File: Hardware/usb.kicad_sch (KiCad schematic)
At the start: 4 parts, among them J3 USB_C_Receptacle_USB2.0

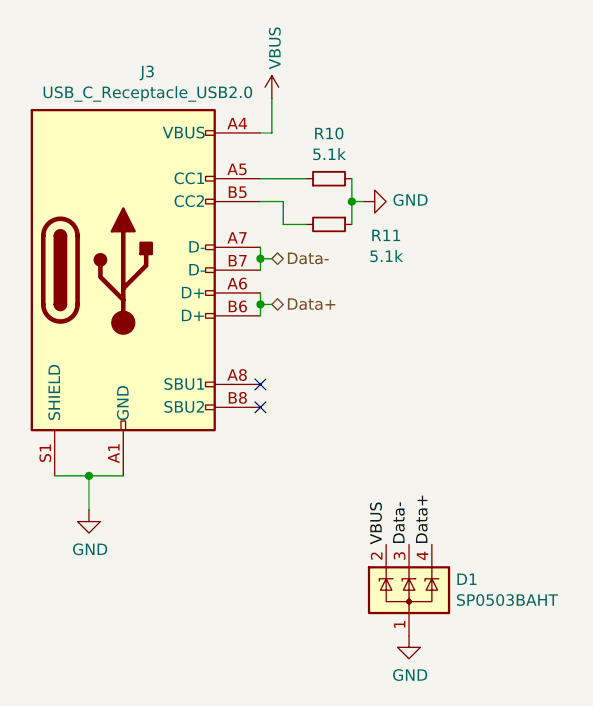
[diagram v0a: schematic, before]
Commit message: Initial changes : removed efuse in place of a current sensor and hardware fuse xt60
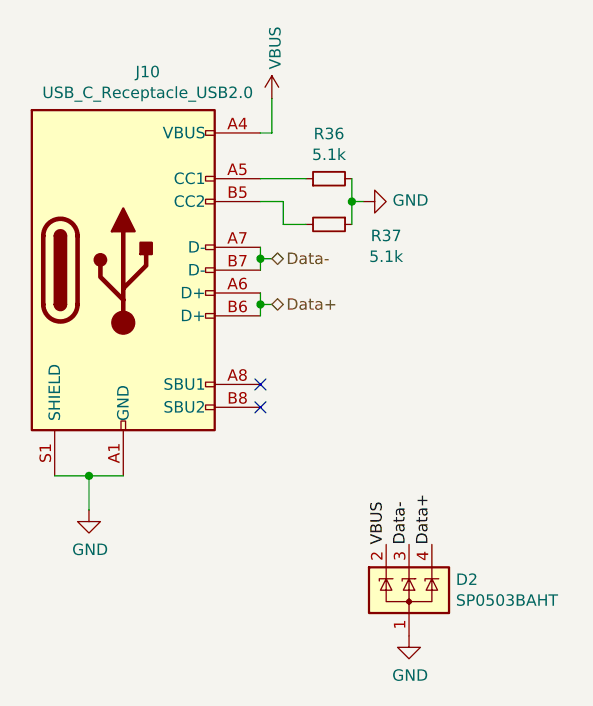
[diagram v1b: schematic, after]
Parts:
- renumbered D1 to D2, J3 to J10, R10 to R36, R11 to R37
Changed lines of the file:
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@@
 (kicad_sch
-	(version 20231120)
+	(version 20250114)
 	(generator "eeschema")
-	(generator_version "8.0")
+	(generator_version "9.0")
 	(paper "A4")
 	(junction
@@
 	(label "Data-"
 		(at 156.464 121.158 90)
-		(fields_autoplaced yes)
 		(effects
 			(font
@@
 	(label "Data+"
 		(at 159.004 121.158 90)
-		(fields_autoplaced yes)
 		(effects
 			(font
@@
 	(label "VBUS"
 		(at 153.924 121.158 90)
-		(fields_autoplaced yes)
 		(effects
 			(font
@@
 		(shape bidirectional)
 		(at 141.224 89.408 0)
-		(fields_autoplaced yes)
 		(effects
 			(font
@@
 		(shape bidirectional)
 		(at 141.224 94.488 0)
-		(fields_autoplaced yes)
 		(effects
 			(font
@@
 		(on_board yes)
 		(dnp no)
-		(property "Reference" "#PWR0129"
+		(property "Reference" "#PWR070"
 			(at 156.464 137.668 0)
 			(effects
@@
 			(project "PDU"
 				(path "/e63e39d7-6ac0-4ffd-8aa3-1841a4541b55/7369ceff-38ea-4740-9245-fda19d5ff608"
-					(reference "#PWR0129")
+					(reference "#PWR070")
 					(unit 1)
 				)
@@
 		(on_board yes)
 		(dnp no)
-		(property "Reference" "#PWR0134"
+		(property "Reference" "#PWR068"
 			(at 141.224 75.438 0)
 			(effects
@@
 			(project "PDU"
 				(path "/e63e39d7-6ac0-4ffd-8aa3-1841a4541b55/7369ceff-38ea-4740-9245-fda19d5ff608"
-					(reference "#PWR0134")
+					(reference "#PWR068")
 					(unit 1)
 				)
@@
 		(on_board yes)
 		(dnp no)
-		(property "Reference" "#PWR0131"
+		(property "Reference" "#PWR069"
 			(at 157.734 83.058 0)
 			(effects
@@
 			(project "PDU"
 				(path "/e63e39d7-6ac0-4ffd-8aa3-1841a4541b55/7369ceff-38ea-4740-9245-fda19d5ff608"
-					(reference "#PWR0131")
+					(reference "#PWR069")
 					(unit 1)
 				)
@@
 		(on_board yes)
 		(dnp no)
-		(property "Reference" "J3"
+		(property "Reference" "J10"
 			(at 127.4318 68.6562 0)
 			(effects
@@
 			(project "PDU"
 				(path "/e63e39d7-6ac0-4ffd-8aa3-1841a4541b55/7369ceff-38ea-4740-9245-fda19d5ff608"
-					(reference "J3")
+					(reference "J10")
 					(unit 1)
 				)
@@
 		(on_board yes)
 		(dnp no)
-		(property "Reference" "R10"
+		(property "Reference" "R36"
 			(at 147.574 75.5396 90)
 			(effects
@@
 			(project "PDU"
 				(path "/e63e39d7-6ac0-4ffd-8aa3-1841a4541b55/7369ceff-38ea-4740-9245-fda19d5ff608"
-					(reference "R10")
+					(reference "R36")
 					(unit 1)
 				)
@@
 		(on_board yes)
 		(dnp no)
-		(property "Reference" "#PWR0126"
+		(property "Reference" "#PWR067"
 			(at 120.904 123.698 0)
 			(effects
@@
 			(project "PDU"
 				(path "/e63e39d7-6ac0-4ffd-8aa3-1841a4541b55/7369ceff-38ea-4740-9245-fda19d5ff608"
-					(reference "#PWR0126")
+					(reference "#PWR067")
 					(unit 1)
 				)
@@
 		(on_board yes)
 		(dnp no)
-		(property "Reference" "R11"
+		(property "Reference" "R37"
 			(at 153.924 86.868 90)
 			(effects
@@
 			(project "PDU"
 				(path "/e63e39d7-6ac0-4ffd-8aa3-1841a4541b55/7369ceff-38ea-4740-9245-fda19d5ff608"
-					(reference "R11")
+					(reference "R37")
 					(unit 1)
 				)
@@
 		(on_board yes)
 		(dnp no)
-		(property "Reference" "D1"
+		(property "Reference" "D2"
 			(at 161.671 125.0696 0)
 			(effects
@@
 			(project "PDU"
 				(path "/e63e39d7-6ac0-4ffd-8aa3-1841a4541b55/7369ceff-38ea-4740-9245-fda19d5ff608"
-					(reference "D1")
+					(reference "D2")
 					(unit 1)
 				)

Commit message: cleaned up schematic and bom
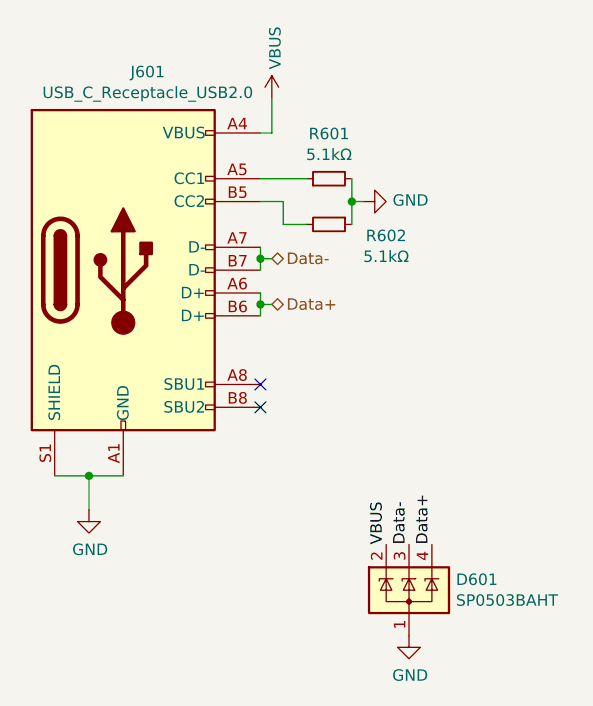
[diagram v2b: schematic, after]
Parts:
- R601: renamed from R36; value 5.1k -> 5.1kΩ
- R602: renamed from R37; value 5.1k -> 5.1kΩ
- renumbered D2 to D601, J10 to J601
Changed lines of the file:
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@@
 		(on_board yes)
 		(dnp no)
-		(property "Reference" "#PWR070"
+		(property "Reference" "#PWR0604"
 			(at 156.464 137.668 0)
 			(effects
@@
 			(project "PDU"
 				(path "/e63e39d7-6ac0-4ffd-8aa3-1841a4541b55/7369ceff-38ea-4740-9245-fda19d5ff608"
-					(reference "#PWR070")
+					(reference "#PWR0604")
 					(unit 1)
 				)
@@
 		(on_board yes)
 		(dnp no)
-		(property "Reference" "#PWR068"
+		(property "Reference" "#PWR0602"
 			(at 141.224 75.438 0)
 			(effects
@@
 			(project "PDU"
 				(path "/e63e39d7-6ac0-4ffd-8aa3-1841a4541b55/7369ceff-38ea-4740-9245-fda19d5ff608"
-					(reference "#PWR068")
+					(reference "#PWR0602")
 					(unit 1)
 				)
@@
 		(on_board yes)
 		(dnp no)
-		(property "Reference" "#PWR069"
+		(property "Reference" "#PWR0603"
 			(at 157.734 83.058 0)
 			(effects
@@
 			(project "PDU"
 				(path "/e63e39d7-6ac0-4ffd-8aa3-1841a4541b55/7369ceff-38ea-4740-9245-fda19d5ff608"
-					(reference "#PWR069")
+					(reference "#PWR0603")
 					(unit 1)
 				)
@@
 		(on_board yes)
 		(dnp no)
-		(property "Reference" "J10"
+		(property "Reference" "J601"
 			(at 127.4318 68.6562 0)
 			(effects
@@
 			(project "PDU"
 				(path "/e63e39d7-6ac0-4ffd-8aa3-1841a4541b55/7369ceff-38ea-4740-9245-fda19d5ff608"
-					(reference "J10")
+					(reference "J601")
 					(unit 1)
 				)
@@
 		(on_board yes)
 		(dnp no)
-		(property "Reference" "R36"
+		(property "Reference" "R601"
 			(at 147.574 75.5396 90)
 			(effects
@@
 			)
 		)
-		(property "Value" "5.1k"
+		(property "Value" "5.1kΩ"
 			(at 147.574 77.851 90)
 			(effects
@@
 			(project "PDU"
 				(path "/e63e39d7-6ac0-4ffd-8aa3-1841a4541b55/7369ceff-38ea-4740-9245-fda19d5ff608"
-					(reference "R36")
+					(reference "R601")
 					(unit 1)
 				)
@@
 		(on_board yes)
 		(dnp no)
-		(property "Reference" "#PWR067"
+		(property "Reference" "#PWR0601"
 			(at 120.904 123.698 0)
 			(effects
@@
 			(project "PDU"
 				(path "/e63e39d7-6ac0-4ffd-8aa3-1841a4541b55/7369ceff-38ea-4740-9245-fda19d5ff608"
-					(reference "#PWR067")
+					(reference "#PWR0601")
 					(unit 1)
 				)
@@
 		(on_board yes)
 		(dnp no)
-		(property "Reference" "R37"
+		(property "Reference" "R602"
 			(at 153.924 86.868 90)
 			(effects
@@
 			)
 		)
-		(property "Value" "5.1k"
+		(property "Value" "5.1kΩ"
 			(at 153.924 89.1794 90)
 			(effects
@@
 			(project "PDU"
 				(path "/e63e39d7-6ac0-4ffd-8aa3-1841a4541b55/7369ceff-38ea-4740-9245-fda19d5ff608"
-					(reference "R37")
+					(reference "R602")
 					(unit 1)
 				)
@@
 		(on_board yes)
 		(dnp no)
-		(property "Reference" "D2"
+		(property "Reference" "D601"
 			(at 161.671 125.0696 0)
 			(effects
@@
 			(project "PDU"
 				(path "/e63e39d7-6ac0-4ffd-8aa3-1841a4541b55/7369ceff-38ea-4740-9245-fda19d5ff608"
-					(reference "D2")
-					(unit 1)
-				)
+					(reference "D601")
+					(unit 1)
+				)
